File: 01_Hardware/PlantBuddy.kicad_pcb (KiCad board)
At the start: 4 copper layers, 35 x 87.3 mm, 56 parts, among them J1 SWD, J2 Conn_I2C_SDA, J3 Conn_I2C_SCL, Q1 AO3401, Q2 AO3400A, SW1 PWR_SW, SW2 BLE_RST_SW, U1 OPT3001, U3 LMC555xM, U5 BlueNRG-M1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

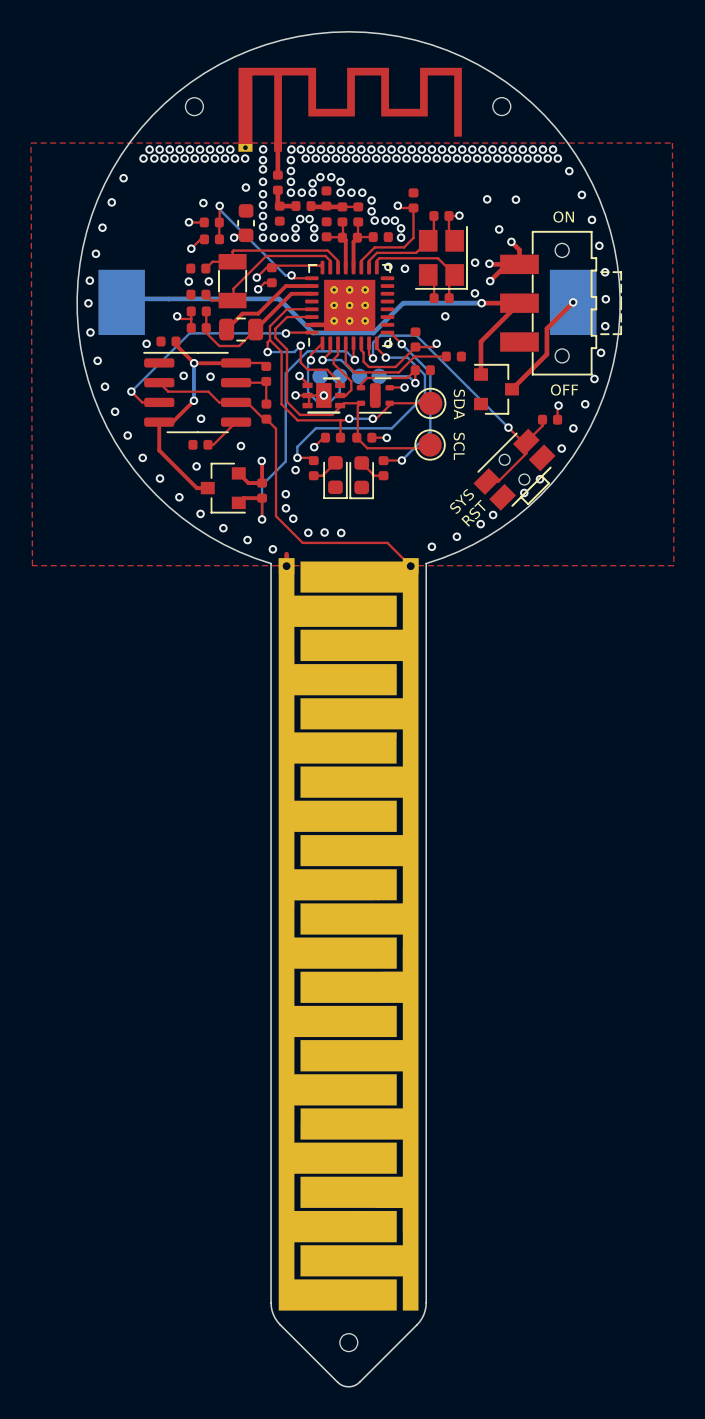
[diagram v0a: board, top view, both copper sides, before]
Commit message: Switched to nRF52810.
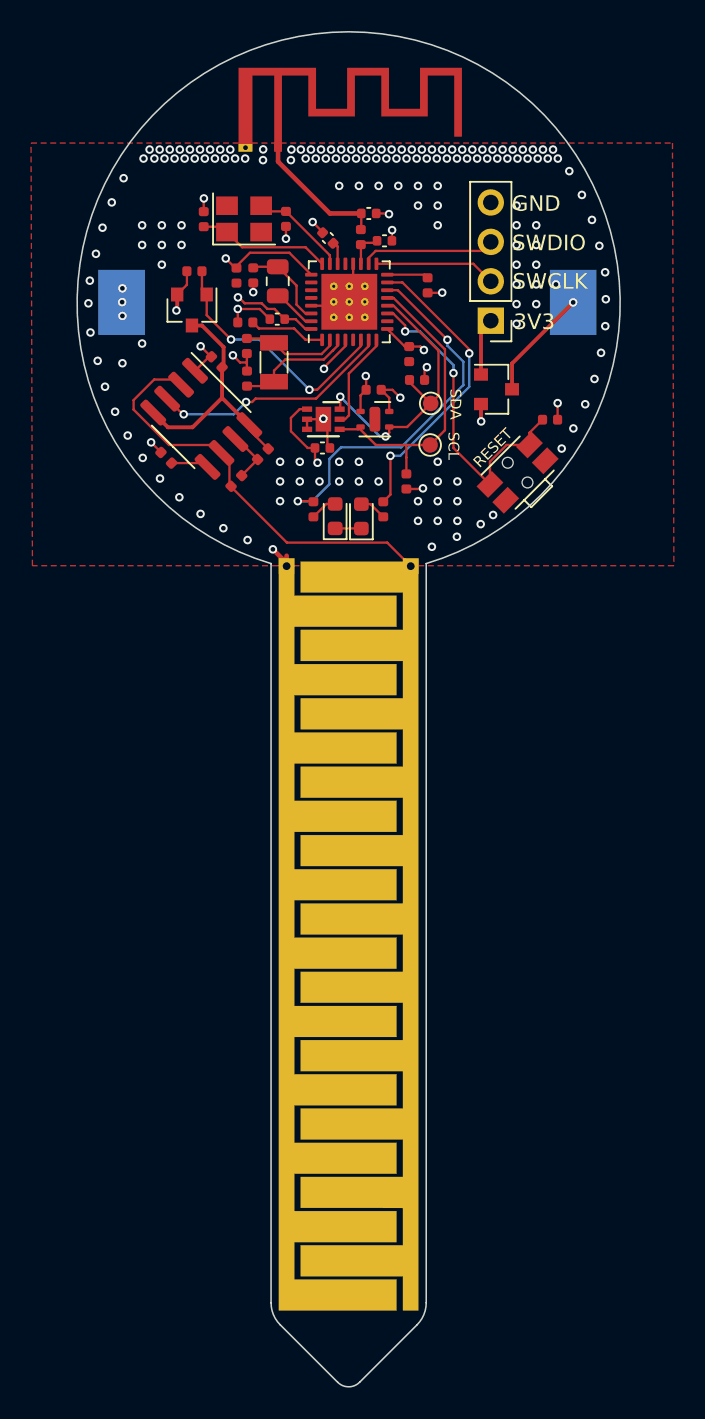
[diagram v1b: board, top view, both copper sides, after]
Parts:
- removed C18: 2.2pF, Capacitor_SMD:C_0402_1005Metric
- removed C19, C20: 1.5pF, Capacitor_SMD:C_0402_1005Metric
- removed C22, C23: 2pF, Capacitor_SMD:C_0402_1005Metric
- removed C26: 20pF, Capacitor_SMD:C_0402_1005Metric
- removed L2: 2.7nH, Inductor_SMD:L_0402_1005Metric
- removed L3: 3.3nH, Inductor_SMD:L_0402_1005Metric
- removed R13: 10k, Resistor_SMD:R_0402_1005Metric
- removed REF** (x3): ToolingHole, PlantBuddy:ToolingHole
- removed SW1: PWR_SW, Button_Switch_SMD:SW_SPDT_CK-JS102011SAQN
- removed U5: BlueNRG-M1, Package_DFN_QFN:QFN-32-1EP_5x5mm_P0.5mm_EP3.3x3.3mm_ThermalVias
- added C15: 4.7uF, Capacitor_SMD:C_0402_1005Metric, F.Cu at (61.1, 65.5)
- added C17: 100nF, Capacitor_SMD:C_0402_1005Metric, F.Cu at (64.0, 73.8)
- added U2: nRF52810-QCxx, Package_DFN_QFN:QFN-32-1EP_5x5mm_P0.5mm_EP3.6x3.6mm_ThermalVias, F.Cu at (65.8, 64.3)
- C13, C14: value 20pF -> 12pF
- C7: value 100nF -> 1.2pF
- C8: value 22uF -> 0.8pF; footprint Capacitor_SMD:C_0603_1608Metric -> Capacitor_SMD:C_0402_1005Metric
- C9: value 100nF -> 100pF
- J1: footprint PlantBuddy:Debug_Connector -> Connector_PinHeader_2.54mm:PinHeader_1x04_P2.54mm_Vertical; moved to F.Cu
- J2, J3: footprint TestPoint:TestPoint_Pad_D1.5mm -> TestPoint:TestPoint_Pad_D1.0mm
- L1: value 2.7nH -> 3.9nH
- Y1: value 16MHz -> 32MHz
- moved C6 16.2 mm to (56.4, 59.0), turned to 270 degrees
- moved R2 14.8 mm to (55.8, 62.4), turned to 0 degrees
- moved R12 14.5 mm to (70.8, 63.3), turned to 90 degrees
- moved Y1 13.0 mm to (59.0, 59.0), turned to 0 degrees
- moved Q1 11.7 mm to (55.6, 64.9), turned to 270 degrees
- moved C11 10.0 mm to (61.7, 59.0), turned to 90 degrees
- moved C10 9.90 mm to (69.6, 67.7), turned to 270 degrees
- moved J1 9.78 mm to (74.9, 65.5)
- moved C8 8.99 mm to (68.0, 60.4), turned to 0 degrees
- moved C7 8.66 mm to (67.0, 58.6), turned to 0 degrees
- moved C13 7.75 mm to (59.2, 69.3), turned to 270 degrees
- moved C9 7.47 mm to (64.4, 60.2), turned to 315 degrees
- moved R15 6.57 mm to (70.1, 69.4), turned to 180 degrees
- moved Y2 5.87 mm to (60.9, 68.2), turned to 270 degrees
- moved R8 5.18 mm to (60.2, 74.2), turned to 225 degrees
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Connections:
- net /FXTAL0 renamed /XC1
- net /FXTAL1 renamed /XC2
- net /SXTAL0 renamed /XL1
- net /SXTAL1 renamed /XL2
- BT1 pad 1: Net-(BT1-Pad1) -> +BATT
- C16 pad 1: Net-(C16-Pad1) -> GND
- C16 pad 2: GND -> Net-(C16-Pad2)
- C5 pad 1: Net-(C16-Pad1) -> GND
- C5 pad 2: GND -> Net-(C5-Pad2)
- C7 pad 1: +BATT -> Net-(AE1-Pad1)
- C8 pad 1: GND -> Net-(C8-Pad1)
- C8 pad 2: +BATT -> GND
- C9 pad 1: Net-(C9-Pad1) -> GND
- C9 pad 2: GND -> Net-(C9-Pad2)
- L1 pad 1: Net-(C18-Pad1) -> Net-(AE1-Pad1)
- L1 pad 2: GND -> Net-(C8-Pad1)
- L4 pad 1: Net-(L4-Pad1) -> Net-(C16-Pad2)
- L4 pad 2: Net-(C16-Pad1) -> Net-(L4-Pad2)
- Q2 pad 1: Net-(BT1-Pad1) -> +BATT
- R12 pad 2: Net-(C9-Pad1) -> Net-(R12-Pad2)
- U6 pad 5: (no net) -> Net-(U6-Pad5)
- Y1 pad 2: GND -> Net-(Y1-Pad2)
- Y1 pad 4: GND -> Net-(Y1-Pad4)
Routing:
- net Net-(BT1-Pad1): track 31.9 -> 0.00 mm, vias 1 -> 0
- net GND: track 16.8 -> 30.5 mm, vias 179 -> 164
- net Net-(C9-Pad1): track 10.2 -> 0.00 mm, vias 2 -> 0
- net Net-(C16-Pad1): track 9.93 -> 0.00 mm
- net /SDA: track 27.7 -> 19.0 mm, vias 4 -> 2
- net Net-(R13-Pad1): track 8.44 -> 0.00 mm
- net /LEDY: track 11.4 -> 19.6 mm
- net /LEDR: track 16.9 -> 24.3 mm
- net Net-(AE1-Pad1): track 1.71 -> 8.65 mm
- net Net-(L4-Pad1): track 6.66 -> 0.00 mm
- net Net-(C16-Pad2): track 0.00 -> 5.74 mm
- net Net-(C5-Pad2): track 0.00 -> 4.93 mm
- net +BATT: track 40.9 -> 36.1 mm
- net Net-(C18-Pad2): track 4.06 -> 0.00 mm
- net Net-(C18-Pad1): track 4.05 -> 0.00 mm
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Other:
- rule pad_to_mask_clearance: 0.05 -> 0.2
- board text added: "RESET"
- board text added: "SWCLK"
- board text added: "SWDIO"
- board text removed: "CLK"
- board text removed: "DIO"
- board text removed: "OFF"
- board text removed: "ON"
- board text removed: "SYS RST"

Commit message: Slight PCB modifications
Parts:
- removed D2: R, LED_SMD:LED_0603_1608Metric
- removed R12: 10k, Resistor_SMD:R_0402_1005Metric
- removed R16: 1k, Resistor_SMD:R_0402_1005Metric
- removed SW2: BLE_RST_SW, Button_Switch_SMD:SW_SPST_EVQP7C
- added R4: 10k, Resistor_SMD:R_0402_1005Metric, F.Cu at (76.0, 67.5)
- J1: value SWD -> SWD+DBG; footprint Connector_PinHeader_2.54mm:PinHeader_1x04_P2.54mm_Vertical -> Connector_PinHeader_2.54mm:PinHeader_2x03_P2.54mm_Vertical
- moved R1 12.8 mm to (70.3, 62.3)
- moved Q2 4.79 mm to (79.2, 67.3)
- moved D1 4.23 mm to (65.7, 74.0), turned to 180 degrees
- moved C17 3.68 mm to (64.0, 70.1)
- moved J1 3.23 mm to (76.4, 62.7)
- moved R3 2.27 mm to (65.7, 77.2), turned to 0 degrees
- moved R15 0.32 mm to (70.4, 69.4)
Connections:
- J1 pad 2: /SWCLK -> /UART_Rx
- J1 pad 3: /SWDIO -> /SWCLK
- J1 pad 4: GND -> /UART_Tx
- Q2 pad 1: +BATT -> Net-(Q2-Pad1)
- R1 pad 2: /~BLE_RST -> Net-(R1-Pad2)
- U2 pad 10: Net-(U2-Pad10) -> /LEDY
- U2 pad 11: /~BLE_RST -> Net-(U2-Pad11)
- U2 pad 14: /LEDR -> /UART_Rx
- U2 pad 15: /LEDY -> /UART_Tx
- U2 pad 16: Net-(R12-Pad2) -> Net-(R1-Pad2)
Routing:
- net /LEDR: track 24.3 -> 0.00 mm, vias 2 -> 0
- net /~BLE_RST: track 21.0 -> 0.00 mm, vias 2 -> 0
- net /UART_Tx: track 0.00 -> 7.20 mm
- net /UART_Rx: track 0.00 -> 6.03 mm
- net Net-(BT1-Pad2): track 7.23 -> 2.91 mm, vias 2 -> 1
- net /LEDY: track 19.6 -> 15.6 mm
- net +BATT: track 36.1 -> 32.4 mm, vias 14 -> 15
- net /SWDIO: track 8.68 -> 11.5 mm, vias 0 -> 2
- net /SWCLK: track 7.84 -> 10.7 mm
- net Net-(R12-Pad2): track 2.68 -> 0.00 mm
- net Net-(Q2-Pad1): track 0.00 -> 2.46 mm
- net Net-(D1-Pad2): track 1.75 -> 3.63 mm
- net Net-(D2-Pad2): track 1.74 -> 0.00 mm
- net Net-(R1-Pad2): track 0.00 -> 1.71 mm
- net GND: track 30.5 -> 30.6 mm, vias 164 -> 175
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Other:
- board text added: "FlivzNexxy"
- board text removed: "3V3"
- board text removed: "GND"
- board text removed: "RESET"
- board text removed: "SCL"
- board text removed: "SDA"
- board text removed: "SWCLK"
- board text removed: "SWDIO"

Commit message: Changed to two-layer PCB
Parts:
- U2: footprint Package_DFN_QFN:QFN-32-1EP_5x5mm_P0.5mm_EP3.6x3.6mm_ThermalVias -> Package_DFN_QFN:QFN-32-1EP_5x5mm_P0.5mm_EP3.6x3.6mm
- moved C15 15.7 mm to (76.4, 69.1), turned to 0 degrees
- moved C7 7.16 mm to (60.6, 55.5), turned to 180 degrees
- moved C9 3.24 mm to (61.5, 58.8)
- moved C6 1.85 mm to (54.7, 59.8)
- moved C8 1.78 mm to (66.3, 60.3), turned to 180 degrees
- moved C11 1.72 mm to (60.2, 59.8)
- moved Y1 1.52 mm to (57.5, 59.0)
- moved L1 1.41 mm to (66.7, 58.8)
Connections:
- U2 pad 10: /LEDY -> /SDA
- U2 pad 11: Net-(U2-Pad11) -> /SCL
- U2 pad 12: /SDA -> /LEDY
- U2 pad 13: /SCL -> Net-(U2-Pad13)
- U2 pad 14: /UART_Rx -> /UART_Tx
- U2 pad 15: /UART_Tx -> /UART_Rx
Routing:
- net +BATT: track 32.4 -> 46.9 mm, vias 15 -> 22
- net /UART_Tx: track 7.20 -> 21.2 mm
- net /UART_Rx: track 6.03 -> 18.9 mm
- net /THR: track 27.3 -> 21.6 mm, vias 0 -> 2
- net Net-(C1-Pad1): track 16.1 -> 20.8 mm, vias 0 -> 2
- net /LEDY: track 15.6 -> 19.4 mm, vias 2 -> 0
- net /~SOIL_EN~: track 16.3 -> 20.0 mm
- net Net-(C9-Pad2): track 1.48 -> 4.58 mm
- net GND: track 30.6 -> 33.2 mm, vias 175 -> 88
- net /XC2: track 8.62 -> 10.8 mm
- net /XC1: track 6.30 -> 7.75 mm
- net Net-(AE1-Pad1): track 8.65 -> 7.59 mm
- net /SWCLK: track 10.7 -> 9.62 mm
- net /SCL: track 20.4 -> 19.4 mm
- net /fHumidity: track 15.6 -> 16.5 mm
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- added copper zone on F.Cu, net +BATT
- added copper zone on B.Cu, net GND
- removed copper zone on In2.Cu, net +BATT
- removed copper zone on In1.Cu, net GND
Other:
- copper layers 4 -> 2
- net class CapacitiveProbe: clearance 0.127 -> 0.152
